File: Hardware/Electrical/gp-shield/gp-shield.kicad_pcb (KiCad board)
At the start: 2 copper layers, 72.4 x 53.3 mm, 209 parts, among them J1 XT60/TERM2, J10 Conn_01x08, J11 Conn_01x04, J12 Conn_01x10, J13 T821-02x08, J14 Conn_01x04, J2 XT60/TERM2, J3 Conn_01x04, J4 Conn_01x03, J5 Conn_01x03, J6 Conn_01x03, J7 Conn_01x03, J8 Conn_01x03, J9 Conn_01x03, Q1 Q_PMOS_GDS, Q3 Q_NMOS_GDS, SW1 SW_SPDT, SW2 SW_Push, SW3 SW_Push, U1 NCP1117-5.0_SOT223, U2 LM4040DBZ-2.5, U4 LM397

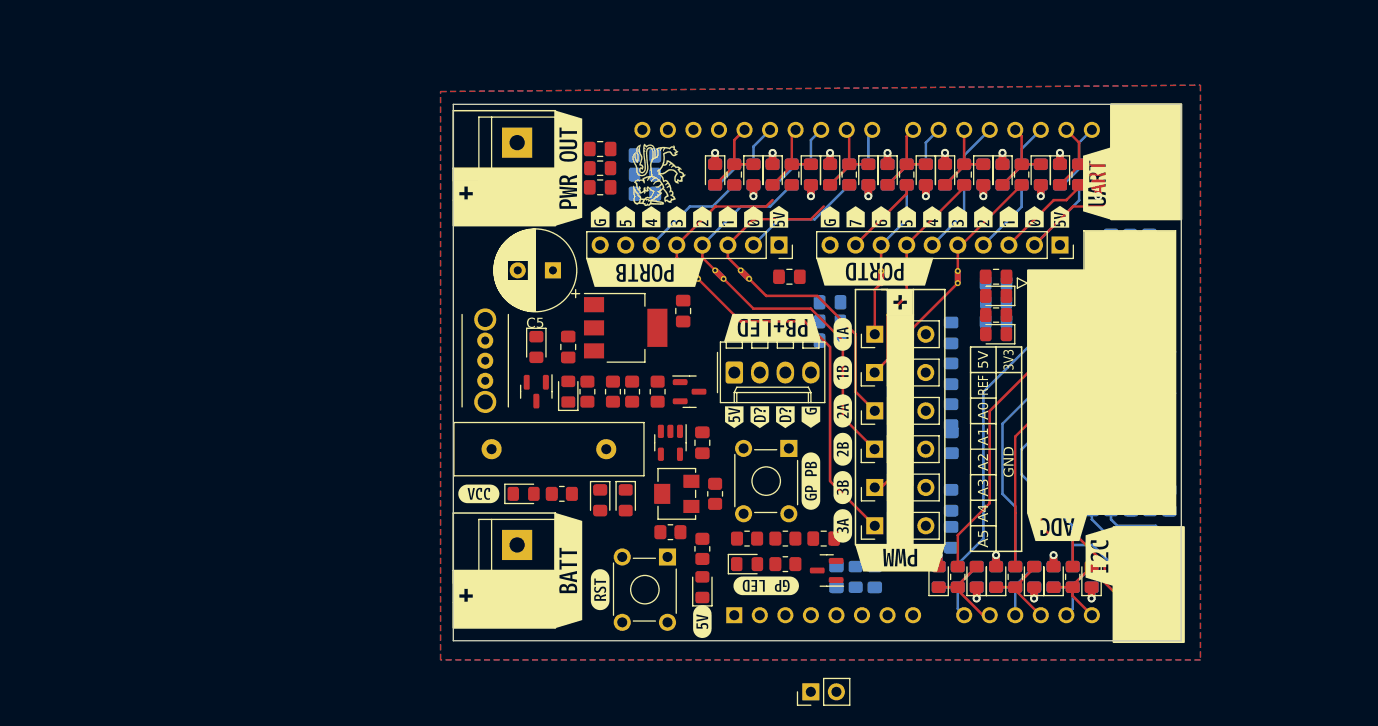
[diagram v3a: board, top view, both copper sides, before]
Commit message: Major PCB changes
Added combined footprint for XT60 and terminal port.
Fixed polarity of Batt and PWR_out connectors.
Standardised polarity markers to show negative on white.
Moved Port D and Port B connectors to be inline with existing arduino connectors. Removed extra pins.
Added analogue in-line output.
Adjusted component placement for more space around power supply and GP PB and LED.
Draft version of track routing - incomplete.
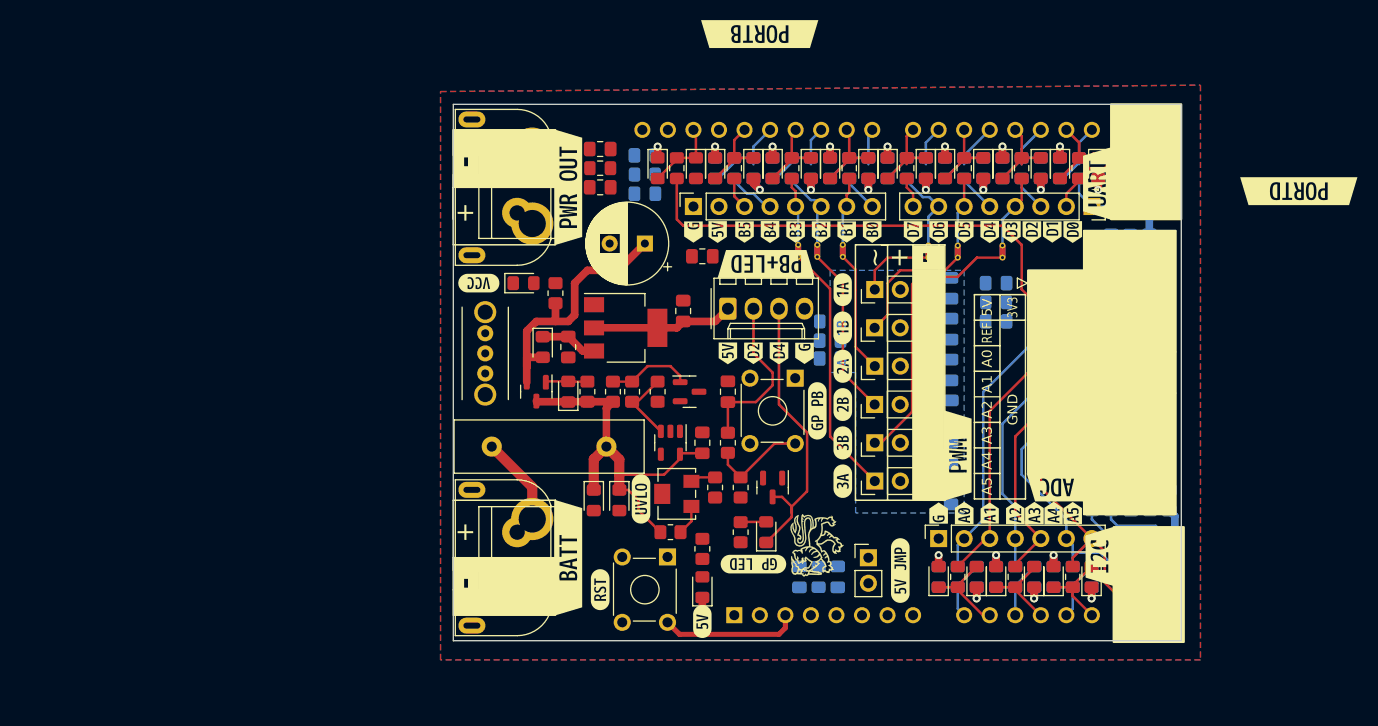
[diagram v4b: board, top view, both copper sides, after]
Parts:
- removed C20: 10u, Capacitor_SMD:C_0805_2012Metric_Pad1.18x1.45mm_HandSolder
- removed C29, C30: 100n, Capacitor_SMD:C_0805_2012Metric_Pad1.18x1.45mm_HandSolder
- removed L8: 22n, Inductor_SMD:L_0805_2012Metric_Pad1.15x1.40mm_HandSolder
- removed kibuzzard-635243F5 (x3): G***, kibuzzard-635243F5
- removed kibuzzard-63524B0B: G***, kibuzzard-63524B0B
- removed kibuzzard-635250A1 (x2): G***, kibuzzard-635250A1
- removed kibuzzard-635250A8 (x2): G***, kibuzzard-635250A8
- removed kibuzzard-635250C3 (x2): G***, kibuzzard-635250C3
- removed kibuzzard-635250C9 (x2): G***, kibuzzard-635250C9
- removed kibuzzard-635250D1 (x2): G***, kibuzzard-635250D1
- removed kibuzzard-635250D8 (x2): G***, kibuzzard-635250D8
- removed kibuzzard-635250DE (x2): G***, kibuzzard-635250DE
- removed kibuzzard-63525119 (x2): G***, kibuzzard-63525119
- removed kibuzzard-6352520C: G***, kibuzzard-6352520C
- removed kibuzzard-63525212: G***, kibuzzard-63525212
- removed kibuzzard-635268A8: G***, kibuzzard-635268A8
- removed kibuzzard-63527DBB: G***, kibuzzard-63527DBB
- removed kibuzzard-63527DC4: G***, kibuzzard-63527DC4
- added J15: Conn_01x07, Connector_PinSocket_2.54mm:PinSocket_1x07_P2.54mm_Vertical, F.Cu at (135.3, 94.6)
- added kibuzzard-636B2900: G***, kibuzzard-636B2900, F.Cu at (119.4, 76.2)
- added kibuzzard-636B290E: G***, kibuzzard-636B290E, F.Cu at (116.8, 76.2)
- added kibuzzard-636B29B0: G***, kibuzzard-636B29B0, F.Cu at (88.3, 99.1)
- added kibuzzard-636B29F7: G***, kibuzzard-636B29F7, F.Cu at (88.3, 57.1)
- added kibuzzard-636B2D3F: G***, kibuzzard-636B2D3F, F.Cu at (134.2, 66.7)
- added kibuzzard-636B37C6: G***, kibuzzard-636B37C6, F.Cu at (142.5, 64.1)
- added kibuzzard-636B37CC: G***, kibuzzard-636B37CC, F.Cu at (140.3, 64.1)
- added kibuzzard-636B37D3: G***, kibuzzard-636B37D3, F.Cu at (137.8, 64.1)
- added kibuzzard-636B37D9: G***, kibuzzard-636B37D9, F.Cu at (135.3, 64.1)
- added kibuzzard-636B37E0: G***, kibuzzard-636B37E0, F.Cu at (132.7, 64.1)
- added kibuzzard-636B37FB: G***, kibuzzard-636B37FB, F.Cu at (128.7, 64.1)
- added kibuzzard-636B3819: G***, kibuzzard-636B3819, F.Cu at (126.1, 64.1)
- added kibuzzard-636B3822: G***, kibuzzard-636B3822, F.Cu at (123.6, 64.1)
- added kibuzzard-636B3829: G***, kibuzzard-636B3829, F.Cu at (121.0, 64.1)
- added kibuzzard-636B3831: G***, kibuzzard-636B3831, F.Cu at (118.5, 64.1)
- added kibuzzard-636B3838: G***, kibuzzard-636B3838, F.Cu at (116.0, 64.1)
- added kibuzzard-636B3843: G***, kibuzzard-636B3843, F.Cu at (113.3, 64.1)
- added kibuzzard-636B3849: G***, kibuzzard-636B3849, F.Cu at (110.9, 64.1)
- added kibuzzard-636B388A: G***, kibuzzard-636B388A, F.Cu at (144.5, 64.1)
- added kibuzzard-636B3891: G***, kibuzzard-636B3891, F.Cu at (146.6, 64.1)
- added kibuzzard-636B38AF: G***, kibuzzard-636B38AF, F.Cu at (148.6, 64.1)
- added kibuzzard-636B3B8D: G***, kibuzzard-636B3B8D, F.Cu at (137.2, 86.4)
- added kibuzzard-636B3BDA: G***, kibuzzard-636B3BDA, F.Cu at (137.8, 92.1)
- added kibuzzard-636B3BFE: G***, kibuzzard-636B3BFE, F.Cu at (148.6, 92.1)
- added kibuzzard-636B3C06: G***, kibuzzard-636B3C06, F.Cu at (146.7, 92.1)
- added kibuzzard-636B3C0D: G***, kibuzzard-636B3C0D, F.Cu at (144.8, 92.1)
- added kibuzzard-636B3C14: G***, kibuzzard-636B3C14, F.Cu at (142.9, 92.1)
- added kibuzzard-636B3C1B: G***, kibuzzard-636B3C1B, F.Cu at (140.3, 92.1)
- added kibuzzard-636B3C68: G***, kibuzzard-636B3C68, F.Cu at (146.8, 89.5)
- added kibuzzard-636B3D37: G***, kibuzzard-636B3D37, F.Cu at (135.3, 92.1)
- added kibuzzard-636B41C3: G***, kibuzzard-636B41C3, F.Cu at (131.4, 97.8)
- added kibuzzard-636B437B: G***, kibuzzard-636B437B, F.Cu at (105.7, 90.7)
- J1, J2: footprint TerminalBlock:TerminalBlock_bornier-2_P5.08mm -> Utility:Combined_TerminalBlock_5.08_XT60_2Row0.2Header
- J12: value Conn_01x10 -> Conn_01x08; footprint Connector_PinSocket_2.54mm:PinSocket_1x10_P2.54mm_Vertical -> Connector_PinSocket_2.54mm:PinSocket_1x08_P2.54mm_Vertical
- moved kibuzzard-635267DD 42.9 mm to (171.1, 60.1)
- moved D36 37.5 mm to (107.3, 57.8), turned to -90 degrees
- moved F17 34.9 mm to (109.2, 57.8), turned to -90 degrees
- moved D37 32.4 mm to (111.1, 57.8), turned to -90 degrees
- moved C19 29.3 mm to (111.8, 66.5)
- moved kibuzzard-635267FD 26.3 mm to (117.5, 44.5)
- moved D5 21.0 mm to (94.0, 69.2)
- moved kibuzzard-635273D0 21.0 mm to (89.5, 69.2), turned to 180 degrees
- moved R14 20.0 mm to (97.2, 70.2), turned to 90 degrees
- moved C8 17.4 mm to (114.3, 80.0), turned to 90 degrees
- moved JP1 14.5 mm to (128.3, 96.5), turned to 0 degrees
- moved R18 11.1 mm to (114.3, 85.1), turned to -90 degrees
- moved NT6 11.1 mm to (121.3, 65.4), turned to -90 degrees
- moved NT8 10.5 mm to (125.7, 65.4), turned to -90 degrees
- moved NT7 10.5 mm to (123.2, 65.4), turned to -90 degrees
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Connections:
- J1 pad 1: GND -> +BATT
- J1 pad 2: +BATT -> GND
- J10 pad 1: +5V_ADC_OUT -> GND
- J10 pad 2: /IO/PORTB0 -> +5V_ADC_OUT
- J10 pad 3: /IO/PORTB1 -> /IO/PORTB5
- J10 pad 4: /IO/PORTB2 -> /IO/PORTB4
- J10 pad 6: /IO/PORTB4 -> /IO/PORTB2
- J10 pad 7: /IO/PORTB5 -> /IO/PORTB1
- J10 pad 8: GND -> /IO/PORTB0
- J12 pad 1: +5V_ADC_OUT -> /IO/PORTD0
- J12 pad 2: /IO/PORTD0 -> /IO/PORTD1
- J12 pad 3: /IO/PORTD1 -> /IO/PORTD2
- J12 pad 4: /IO/PORTD2 -> /IO/PORTD3
- J12 pad 5: /IO/PORTD3 -> /IO/PORTD4
- J12 pad 6: /IO/PORTD4 -> /IO/PORTD5
- J12 pad 7: /IO/PORTD5 -> /IO/PORTD6
- J12 pad 8: /IO/PORTD6 -> /IO/PORTD7
- J13 pad 2: +3V3_ADC_OUT -> GND
- J3 pad 2: /MCU/LED_OUT -> /IO/PORTD4
- J3 pad 3: /IO/PORTD4 -> /MCU/LED_OUT
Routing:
- net /IO/ADC.AREF: track 0.00 -> 46.5 mm
- net /Power/+BATT_FUSED: track 0.00 -> 37.9 mm
- net /MCU/LED_OUT: track 0.00 -> 29.0 mm
- net VCC: track 0.00 -> 26.6 mm
- net +5V: track 22.7 -> 45.6 mm, vias 10 -> 11
- net +5V_I2C_OUT: track 0.00 -> 14.8 mm
- net /MCU/~{RESET}: track 0.00 -> 13.7 mm
- net /IO/PORTD4: track 7.30 -> 20.4 mm
- net /IO/PORTD0: track 20.1 -> 8.28 mm
- net /IO/PWM.C0: track 35.5 -> 25.5 mm
- net /MCU/GP_SW: track 0.00 -> 9.79 mm
- net /IO/PWM.B1: track 26.5 -> 17.0 mm
- net /IO/PWM.B0: track 21.3 -> 12.2 mm
- net +BATT: track 0.00 -> 8.87 mm
- net /Power/VCC_VREF: track 0.00 -> 8.34 mm
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- added copper zone on B.Cu, net +5V_PWM_OUT
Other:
- board text added: "+"
- board text added: "6V->20V"
- board text added: "~"

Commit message: Complete draft PCB layout
Added updated renders to doc.
Added some documentation to schematic
complete PCB layout with some revisions still needed
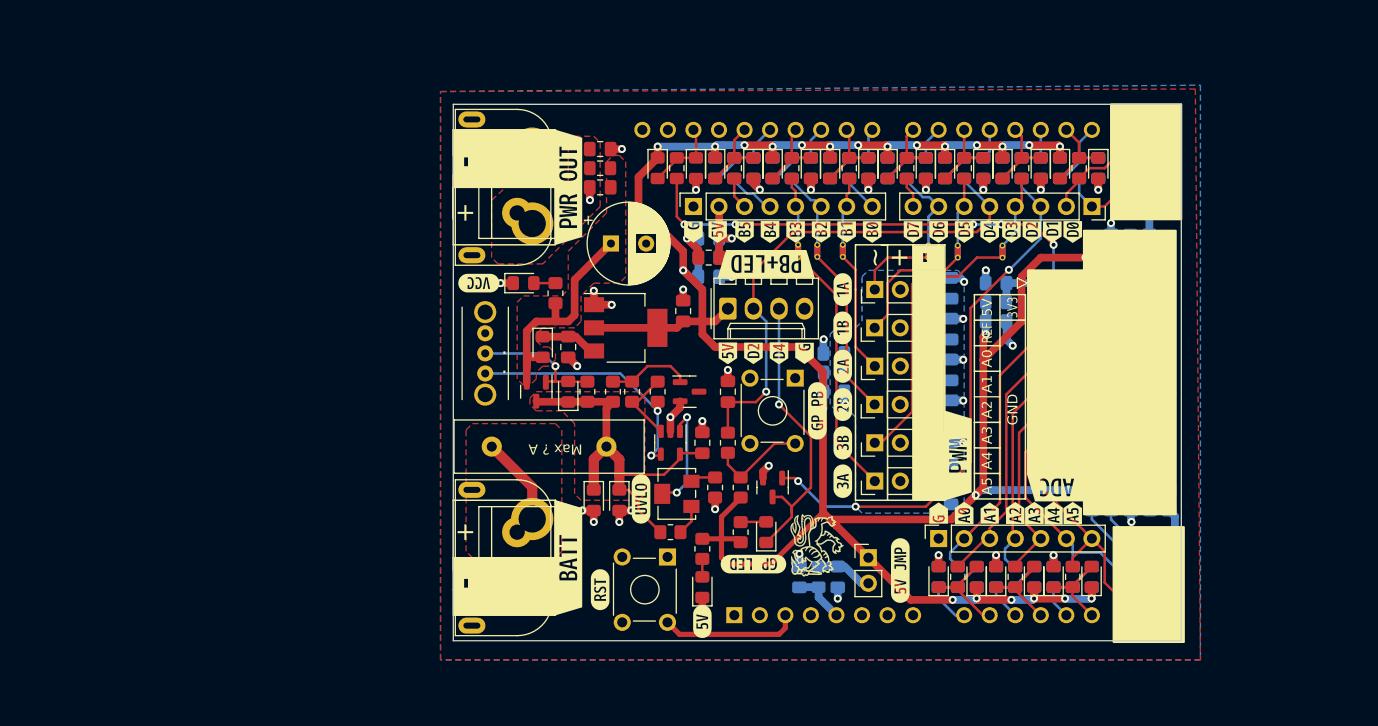
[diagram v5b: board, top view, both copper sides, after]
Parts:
- removed kibuzzard-635257F8: G***, kibuzzard-635257F8
- removed kibuzzard-635267DD: G***, kibuzzard-635267DD
- removed kibuzzard-635267FD: G***, kibuzzard-635267FD
- removed kibuzzard-63526951: G***, kibuzzard-63526951
- added kibuzzard-636C5470: G***, kibuzzard-636C5470, B.Cu at (154.3, 69.2)
- added kibuzzard-636C54A9: G***, kibuzzard-636C54A9, B.Cu at (154.3, 87.0)
- R1: value 100K -> 22k
- R2: value 100K -> 5k6
- R3: value 100K -> 10k
- R4: value 100K -> 1k
- R9: value 100K -> 40k
- RV1: value R_Potentiometer -> 10k
- moved C23 13.6 mm to (112.4, 68.6), turned to 0 degrees
- moved L5 10.4 mm to (112.4, 66.7), turned to 180 degrees
- moved C24 7.75 mm to (112.4, 64.8), turned to 180 degrees
- moved L3 5.09 mm to (124.8, 78.1), turned to 0 degrees
- moved C5 3.37 mm to (102.7, 65.3), turned to 0 degrees
- moved C18 3.32 mm to (124.8, 80.0), turned to 0 degrees
- moved C17 1.33 mm to (124.8, 76.2), turned to 180 degrees
- moved C19 0.65 mm to (112.4, 66.7)
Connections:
- C19 pad 1: +5V_ADC_OUT -> +5V_GPIO_OUT
- J10 pad 2: +5V_ADC_OUT -> +5V_GPIO_OUT
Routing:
- net +5V: track 45.6 -> 264.2 mm, vias 11 -> 25
- net /IO/PORTD2: track 3.57 -> 53.7 mm, vias 0 -> 3
- net GND: track 23.1 -> 72.1 mm, vias 11 -> 46
- net /IO/PORTD4: track 20.4 -> 50.5 mm, vias 0 -> 1
- net /Power/VCC_CMP_OUT: track 0.00 -> 25.3 mm, vias 0 -> 2
- net /Power/VCC_CMP-: track 0.00 -> 11.1 mm, vias 0 -> 2
- net +5V_GPIO_OUT: track 0.00 -> 9.53 mm, vias 0 -> 1
- net /Power/VCC_EN: track 4.18 -> 13.2 mm, vias 0 -> 1
- net /MCU/+5V_JMP: track 0.00 -> 5.65 mm
- net +5V_ARDUINO: track 0.00 -> 5.43 mm
- net +5V_ADC_OUT: track 0.00 -> 5.34 mm
- net VCC: track 26.6 -> 23.5 mm
- net /IO/ADC.AREF: track 46.5 -> 49.3 mm, vias 0 -> 5
- net /Power/VCC_LED: track 0.00 -> 2.15 mm
- net /Power/5V_LED: track 0.00 -> 1.78 mm
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- added copper zone on F.Cu, net +BATT
- added copper zone on F.Cu, net /Power/+BATT_FUSED
- added copper zone on F.Cu, net VCC
- added copper zone on F.Cu, net VCC_OUT
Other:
- board text added: "."
- board text added: "Max ? A"

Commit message: Minor changes to silkscreen and documentation
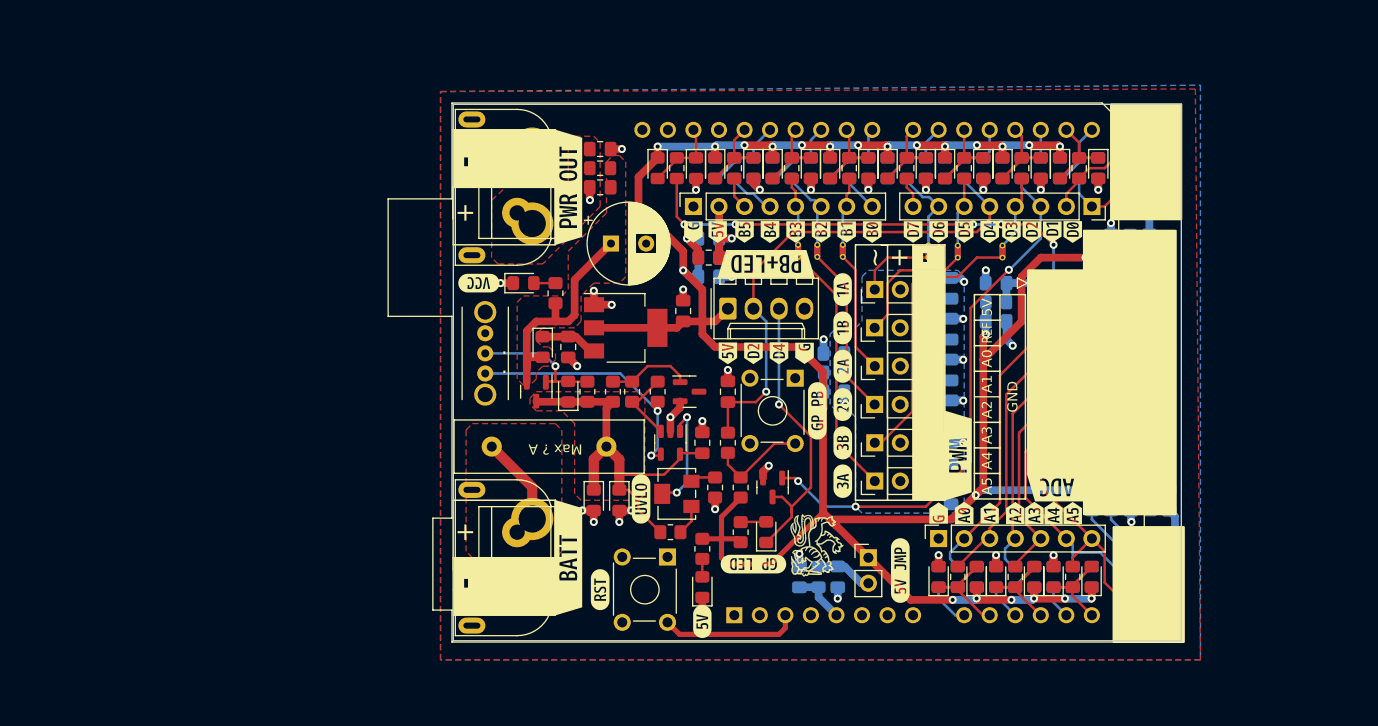
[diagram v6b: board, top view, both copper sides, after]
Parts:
- removed kibuzzard-63527AB4: G***, kibuzzard-63527AB4
- removed kibuzzard-63527AC9: G***, kibuzzard-63527AC9
- removed kibuzzard-63527AF1 (x2): G***, kibuzzard-63527AF1
- removed kibuzzard-63527AF8 (x2): G***, kibuzzard-63527AF8
- removed kibuzzard-63527B1E: G***, kibuzzard-63527B1E
- removed kibuzzard-63527B27: G***, kibuzzard-63527B27
- added kibuzzard-636C5C0D: G***, kibuzzard-636C5C0D, B.Cu at (153.0, 53.3)
- added kibuzzard-636C5C1C: G***, kibuzzard-636C5C1C, B.Cu at (153.0, 61.0)
- added kibuzzard-636C5C28: G***, kibuzzard-636C5C28, B.Cu at (153.0, 58.4)
- added kibuzzard-636C5C36: G***, kibuzzard-636C5C36, B.Cu at (153.0, 55.9)
- added kibuzzard-636C5C4A: G***, kibuzzard-636C5C4A, B.Cu at (153.0, 97.8)
- added kibuzzard-636C5C55: G***, kibuzzard-636C5C55, B.Cu at (153.0, 95.2)
- added kibuzzard-636C5C62: G***, kibuzzard-636C5C62, B.Cu at (153.0, 100.3)
- added kibuzzard-636C5C70: G***, kibuzzard-636C5C70, B.Cu at (153.0, 102.9)
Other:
- board text removed: "3V3"
